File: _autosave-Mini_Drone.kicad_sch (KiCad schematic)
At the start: 67 parts, among them J1 Conn_01x02, J3 Conn_01x02, J4 Conn_01x06, J7 Conn_01x11, J8 Conn_01x11, Q1 AO3400A, Q2 AO3400A, Q3 AO3400A, Q4 AO3400A, SW2 Tactile Switch 3x4x2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

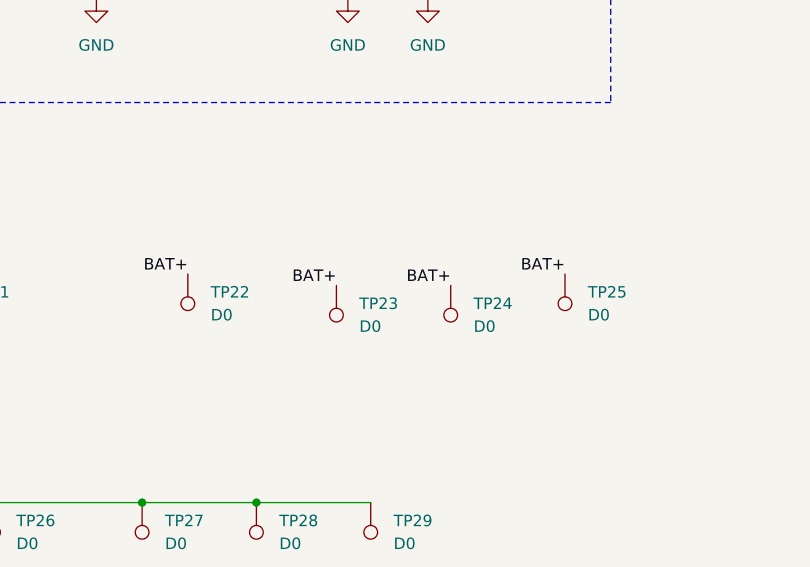
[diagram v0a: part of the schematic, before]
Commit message: without motor driver silkscreen and neeed to make the routing a bit clearer and check the thickness
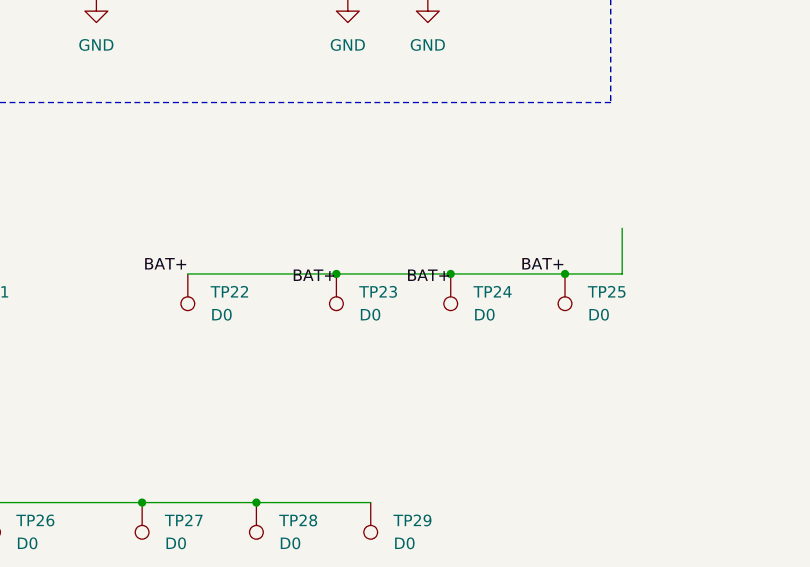
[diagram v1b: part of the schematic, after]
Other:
- moved on the sheet: TP23, TP24
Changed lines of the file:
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@@
 	)
 	(junction
+		(at 102.87 121.92)
+		(diameter 0)
+		(color 0 0 0 0)
+	)
+	(junction
 		(at 95.25 264.16)
 		(diameter 0)
@@
 	)
 	(junction
+		(at 115.57 121.92)
+		(diameter 0)
+		(color 0 0 0 0)
+	)
+	(junction
 		(at 81.28 147.32)
 		(diameter 0)
@@
 	)
 	(junction
+		(at 128.27 121.92)
+		(diameter 0)
+		(color 0 0 0 0)
+	)
+	(junction
 		(at 149.86 236.22)
 		(diameter 0)
@@
 	(wire
 		(pts
+			(xy 86.36 121.92) (xy 102.87 121.92)
+		)
+		(stroke
+			(width 0)
+			(type default)
+		)
+	)
+	(wire
+		(pts
 			(xy 256.54 40.64) (xy 262.89 40.64)
 		)
@@
 	(wire
 		(pts
+			(xy 134.62 116.84) (xy 134.62 121.92)
+		)
+		(stroke
+			(width 0)
+			(type default)
+		)
+	)
+	(wire
+		(pts
 			(xy 113.03 82.55) (xy 113.03 76.2)
 		)
@@
 	(wire
 		(pts
+			(xy 115.57 121.92) (xy 128.27 121.92)
+		)
+		(stroke
+			(width 0)
+			(type default)
+		)
+	)
+	(wire
+		(pts
 			(xy 49.53 81.28) (xy 45.72 81.28)
 		)
@@
 	(wire
 		(pts
+			(xy 128.27 121.92) (xy 134.62 121.92)
+		)
+		(stroke
+			(width 0)
+			(type default)
+		)
+	)
+	(wire
+		(pts
 			(xy 313.69 39.37) (xy 313.69 43.18)
 		)
@@
 	(wire
 		(pts
+			(xy 102.87 121.92) (xy 115.57 121.92)
+		)
+		(stroke
+			(width 0)
+			(type default)
+		)
+	)
+	(wire
+		(pts
 			(xy 195.58 265.43) (xy 200.66 265.43)
 		)
@@
 		(length 2.54)
 		(shape round)
+		(at 134.62 116.84 0)
+		(fields_autoplaced yes)
+		(effects
+			(font
+				(size 1.27 1.27)
+			)
+			(justify left bottom)
+		)
+		(property "Netclass" "power"
+			(at 135.3185 114.3 0)
+			(effects
+				(font
+					(size 1.27 1.27)
+				)
+				(justify left)
+			)
+		)
+		(property "Component Class" ""
+			(at -162.56 13.97 0)
+			(effects
+				(font
+					(size 1.27 1.27)
+					(italic yes)
+				)
+			)
+		)
+	)
+	(netclass_flag ""
+		(length 2.54)
+		(shape round)
 		(at 195.58 243.84 270)
 		(fields_autoplaced yes)
@@
 		(exclude_from_sim no)
 		(in_bom yes)
-		(on_board yes)
+		(on_board no)
 		(dnp no)
 		(property "Reference" "R7"
@@
 		(exclude_from_sim no)
 		(in_bom yes)
-		(on_board yes)
+		(on_board no)
 		(dnp no)
 		(property "Reference" "C6"
@@
 		(exclude_from_sim no)
 		(in_bom yes)
-		(on_board yes)
+		(on_board no)
 		(dnp no)
 		(fields_autoplaced yes)
@@
 	(symbol
 		(lib_id "Connector:TestPoint")
-		(at 102.87 123.19 180)
+		(at 102.87 121.92 180)
 		(unit 1)
 		(exclude_from_sim no)
@@
 		(fields_autoplaced yes)
 		(property "Reference" "TP23"
-			(at 105.41 125.2219 0)
+			(at 105.41 123.9519 0)
 			(effects
 				(font
@@
 		)
 		(property "Value" "D0"
-			(at 105.41 127.7619 0)
+			(at 105.41 126.4919 0)
 			(effects
 				(font
@@
 		)
 		(property "Footprint" "TestPoint:TestPoint_THTPad_2.0x2.0mm_Drill1.0mm"
-			(at 97.79 123.19 0)
+			(at 97.79 121.92 0)
 			(effects
 				(font
@@
 		)
 		(property "Datasheet" "~"
-			(at 97.79 123.19 0)
+			(at 97.79 121.92 0)
 			(effects
 				(font
@@
 		)
 		(property "Description" "test point"
-			(at 102.87 123.19 0)
+			(at 102.87 121.92 0)
 			(effects
 				(font
@@
 		(exclude_from_sim no)
 		(in_bom yes)
-		(on_board yes)
+		(on_board no)
 		(dnp no)
 		(property "Reference" "TP15"
@@
 		(exclude_from_sim no)
 		(in_bom yes)
-		(on_board yes)
+		(on_board no)
 		(dnp no)
 		(fields_autoplaced yes)
@@
 		(exclude_from_sim no)
 		(in_bom yes)
-		(on_board yes)
+		(on_board no)
 		(dnp no)
 		(fields_autoplaced yes)
@@
 		(exclude_from_sim no)
 		(in_bom yes)
-		(on_board yes)
+		(on_board no)
 		(dnp no)
 		(property "Reference" "TP11"
@@
 		(exclude_from_sim no)
 		(in_bom yes)
-		(on_board yes)
+		(on_board no)
 		(dnp no)
 		(fields_autoplaced yes)
@@
 		(exclude_from_sim no)
 		(in_bom yes)
-		(on_board yes)
+		(on_board no)
 		(dnp no)
 		(property "Reference" "TP5"
@@
 		(exclude_from_sim no)
 		(in_bom yes)
-		(on_board yes)
+		(on_board no)
 		(dnp no)
 		(property "Reference" "C1"
@@
 		(exclude_from_sim no)
 		(in_bom yes)
-		(on_board yes)
+		(on_board no)
 		(dnp no)
 		(fields_autoplaced yes)
@@
 		(exclude_from_sim no)
 		(in_bom yes)
-		(on_board yes)
+		(on_board no)
 		(dnp no)
 		(fields_autoplaced yes)
@@
 		(exclude_from_sim no)
 		(in_bom yes)
-		(on_board yes)
+		(on_board no)
 		(dnp no)
 		(fields_autoplaced yes)
@@
 		(exclude_from_sim no)
 		(in_bom yes)
-		(on_board yes)
+		(on_board no)
 		(dnp no)
 		(fields_autoplaced yes)
@@
 		(exclude_from_sim no)
 		(in_bom yes)
-		(on_board yes)
+		(on_board no)
 		(dnp no)
 		(fields_autoplaced yes)
@@
 		(exclude_from_sim no)
 		(in_bom yes)
-		(on_board yes)
+		(on_board no)
 		(dnp no)
 		(fields_autoplaced yes)
@@
 		(exclude_from_sim no)
 		(in_bom yes)
-		(on_board yes)
+		(on_board no)
 		(dnp no)
 		(property "Reference" "C7"
@@
 		(exclude_from_sim no)
 		(in_bom yes)
-		(on_board yes)
+		(on_board no)
 		(dnp no)
 		(fields_autoplaced yes)
@@
 		(exclude_from_sim no)
 		(in_bom yes)
-		(on_board yes)
+		(on_board no)
 		(dnp no)
 		(fields_autoplaced yes)
@@
 		(exclude_from_sim no)
 		(in_bom yes)
-		(on_board yes)
+		(on_board no)
 		(dnp no)
 		(fields_autoplaced yes)
@@
 		(exclude_from_sim no)
 		(in_bom yes)
-		(on_board yes)
+		(on_board no)
 		(dnp no)
 		(property "Reference" "R4"
@@
 		(exclude_from_sim no)
 		(in_bom yes)
-		(on_board yes)
+		(on_board no)
 		(dnp no)
 		(property "Reference" "R5"
@@
 		(exclude_from_sim no)
 		(in_bom yes)
-		(on_board yes)
+		(on_board no)
 		(dnp no)
 		(fields_autoplaced yes)
@@
 		(exclude_from_sim no)
 		(in_bom yes)
-		(on_board yes)
+		(on_board no)
 		(dnp no)
 		(property "Reference" "TP16"
@@
 		(exclude_from_sim no)
 		(in_bom yes)
-		(on_board yes)
+		(on_board no)
 		(dnp no)
 		(fields_autoplaced yes)
@@
 		(exclude_from_sim no)
 		(in_bom yes)
-		(on_board yes)
+		(on_board no)
 		(dnp no)
 		(fields_autoplaced yes)
@@
 		(exclude_from_sim no)
 		(in_bom yes)
-		(on_board yes)
+		(on_board no)
 		(dnp no)
 		(fields_autoplaced yes)
@@
 		(exclude_from_sim no)
 		(in_bom yes)
-		(on_board yes)
+		(on_board no)
 		(dnp no)
 		(fields_autoplaced yes)
@@
 		(exclude_from_sim no)
 		(in_bom yes)
-		(on_board yes)
+		(on_board no)
 		(dnp no)
 		(property "Reference" "R6"
@@
 		(exclude_from_sim no)
 		(in_bom yes)
-		(on_board yes)
+		(on_board no)
 		(dnp no)
 		(fields_autoplaced yes)
@@
 		(exclude_from_sim no)
 		(in_bom yes)
-		(on_board yes)
+		(on_board no)
 		(dnp no)
 		(fields_autoplaced yes)
@@
 		(exclude_from_sim no)
 		(in_bom yes)
-		(on_board yes)
+		(on_board no)
 		(dnp no)
 		(fields_autoplaced yes)
@@
 		(exclude_from_sim no)
 		(in_bom yes)
-		(on_board yes)
+		(on_board no)
 		(dnp no)
 		(property "Reference" "C5"
@@
 	(symbol
 		(lib_id "Connector:TestPoint")
-		(at 115.57 123.19 180)
+		(at 115.57 121.92 180)
 		(unit 1)
 		(exclude_from_sim no)
@@
 		(fields_autoplaced yes)
 		(property "Reference" "TP24"
-			(at 118.11 125.2219 0)
+			(at 118.11 123.9519 0)
 			(effects
 				(font
@@
 		)
 		(property "Value" "D0"
-			(at 118.11 127.7619 0)
+			(at 118.11 126.4919 0)
 			(effects
 				(font
@@
 		)
 		(property "Footprint" "TestPoint:TestPoint_THTPad_2.0x2.0mm_Drill1.0mm"
-			(at 110.49 123.19 0)
+			(at 110.49 121.92 0)
 			(effects
 				(font
@@
 		)
 		(property "Datasheet" "~"
-			(at 110.49 123.19 0)
+			(at 110.49 121.92 0)
 			(effects
 				(font
@@
 		)
 		(property "Description" "test point"
-			(at 115.57 123.19 0)
+			(at 115.57 121.92 0)
 			(effects
 				(font
@@
 		(exclude_from_sim no)
 		(in_bom yes)
-		(on_board yes)
+		(on_board no)
 		(dnp no)
 		(fields_autoplaced yes)
@@
 		(exclude_from_sim no)
 		(in_bom yes)
-		(on_board yes)
+		(on_board no)
 		(dnp no)
 		(fields_autoplaced yes)
@@
 		(exclude_from_sim no)
 		(in_bom yes)
-		(on_board yes)
+		(on_board no)
 		(dnp no)
 		(fields_autoplaced yes)
@@
 		(exclude_from_sim no)
 		(in_bom yes)
-		(on_board yes)
+		(on_board no)
 		(dnp no)
 		(property "Reference" "TP17"
